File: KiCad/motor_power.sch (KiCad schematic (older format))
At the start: 28 parts

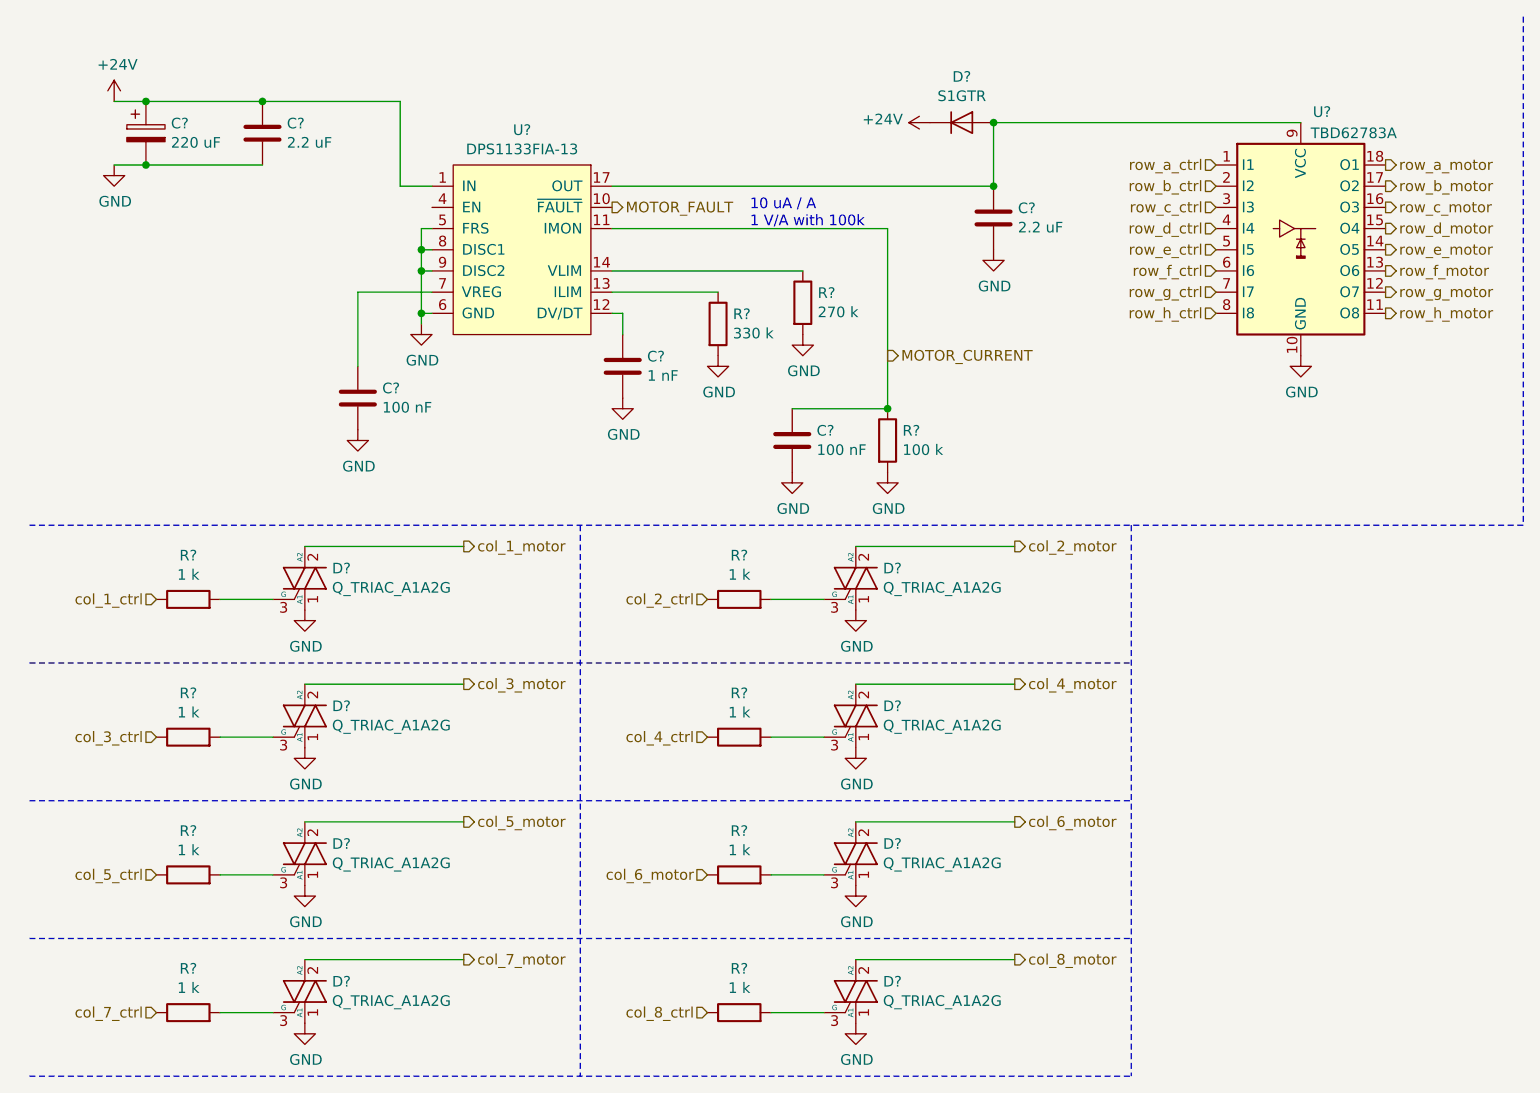
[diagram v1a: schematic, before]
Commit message: Fixing ERC rules
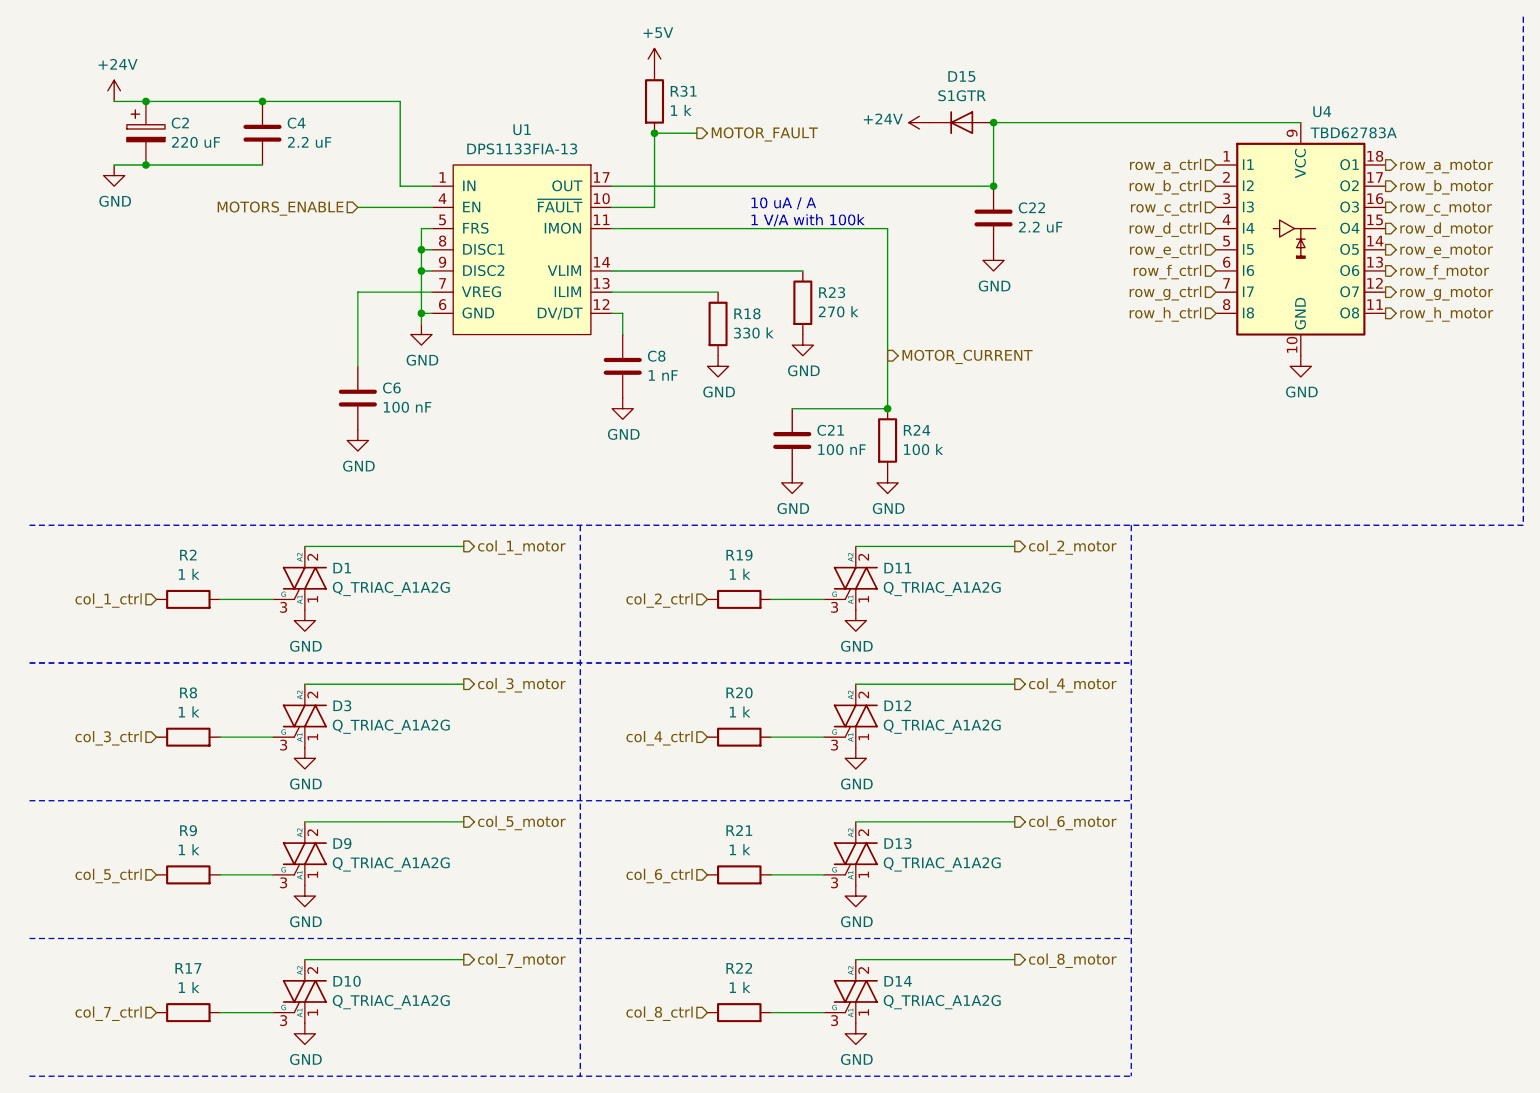
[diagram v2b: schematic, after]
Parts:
- added R31: 1 k, symbol Device:R
- gave numbers to parts that had none: 28
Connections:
- net MOTOR_FAULT: now also R31.2
- net col_6_motor: no longer R21.1
- net MOTORS_ENABLE: now reaches U1.4 (EN)
- new net +5V: R31.1
- new net col_6_ctrl: R21.1

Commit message: Current WIP for board layout
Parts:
- removed C2: 220 uF, symbol Device:CP
- added C2: 22 uF, Capacitor_SMD:C_1210_3225Metric_Pad1.42x2.65mm_HandSolder, symbol Device:C
- C21, C22, C4, C6, C8: footprint (none) -> Capacitor_SMD:C_0603_1608Metric_Pad1.05x0.95mm_HandSolder
- D1, D10, D11, D12, D13, D14, D3, D9: footprint (none) -> Package_TO_SOT_SMD:SOT-223-3_TabPin2
- D15: footprint (none) -> Diode_SMD:D_SMA_Handsoldering
- R17, R18, R19, R2, R20, R21, R22, R23, R24, R31, R8, R9: footprint (none) -> Resistor_SMD:R_0603_1608Metric_Pad1.05x0.95mm_HandSolder
- U1: footprint kicad_pcb:QFN-17-Diodes1 -> Snack Machine:DPS1133FIA-13
- U4: footprint (none) -> Package_SO:SSOP-18_4.4x6.5mm_P0.65mm
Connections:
- net +24V: now also C2.1
- net GND: now also C2.2
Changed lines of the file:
@@
 F 0 "U4" H 6550 2000 50  0000 C CNN
 F 1 "TBD62783A" H 6700 1900 50  0000 C CNN
-F 2 "" H 6450 900 50  0001 C CNN
+F 2 "Package_SO:SSOP-18_4.4x6.5mm_P0.65mm" H 6450 900 50  0001 C CNN
 F 3 "http://toshiba.semicon-storage.com/info/docget.jsp?did=30523&prodName=TBD62783APG" H 6150 1850 50  0001 C CNN
 	1    6450 1450
@@
 F 0 "U1" H 2775 1315 50  0000 C CNN
 F 1 "DPS1133FIA-13" H 2775 1224 50  0000 C CNN
-F 2 "kicad_pcb:QFN-17-Diodes1" H 2450 1200 50  0001 L CNN
+F 2 "Snack Machine:DPS1133FIA-13" H 2450 1200 50  0001 L CNN
 F 3 "" V 2700 1150 50  0001 C CNN
 	1    2450 1150
@@
 F 0 "C4" H 1665 1046 50  0000 L CNN
 F 1 "2.2 uF" H 1665 955 50  0000 L CNN
-F 2 "" H 1588 850 50  0001 C CNN
+F 2 "Capacitor_SMD:C_0603_1608Metric_Pad1.05x0.95mm_HandSolder" H 1588 850 50  0001 C CNN
 F 3 "~" H 1550 1000 50  0001 C CNN
 	1    1550 1000
@@
 $EndComp
 Wire Wire Line
-	850  850  1000 850
-Wire Wire Line
-	850  1150 1000 1150
-$Comp
-L Device:CP C2
-U 1 1 5DBC5CDD
-P 1000 1000
-F 0 "C2" H 1118 1046 50  0000 L CNN
-F 1 "220 uF" H 1118 955 50  0000 L CNN
-F 2 "" H 1038 850 50  0001 C CNN
-F 3 "~" H 1000 1000 50  0001 C CNN
-	1    1000 1000
-	1    0    0    -1
-$EndComp
-Connection ~ 1000 850
-Wire Wire Line
-	1000 850  1550 850
-Connection ~ 1000 1150
-Wire Wire Line
-	1000 1150 1550 1150
-Wire Wire Line
 	1550 850  2200 850
 Wire Wire Line
@@
 F 0 "C6" H 2115 2296 50  0000 L CNN
 F 1 "100 nF" H 2115 2205 50  0000 L CNN
-F 2 "" H 2038 2100 50  0001 C CNN
+F 2 "Capacitor_SMD:C_0603_1608Metric_Pad1.05x0.95mm_HandSolder" H 2038 2100 50  0001 C CNN
 F 3 "~" H 2000 2250 50  0001 C CNN
 	1    2000 2250
@@
 F 0 "C8" H 3365 2146 50  0000 L CNN
 F 1 "1 nF" H 3365 2055 50  0000 L CNN
-F 2 "" H 3288 1950 50  0001 C CNN
+F 2 "Capacitor_SMD:C_0603_1608Metric_Pad1.05x0.95mm_HandSolder" H 3288 1950 50  0001 C CNN
 F 3 "~" H 3250 2100 50  0001 C CNN
 	1    3250 2100
@@
 F 0 "R18" H 3770 1946 50  0000 L CNN
 F 1 "330 k" H 3770 1855 50  0000 L CNN
-F 2 "" V 3630 1900 50  0001 C CNN
+F 2 "Resistor_SMD:R_0603_1608Metric_Pad1.05x0.95mm_HandSolder" V 3630 1900 50  0001 C CNN
 F 3 "~" H 3700 1900 50  0001 C CNN
 	1    3700 1900
@@
 F 0 "R23" H 4170 1846 50  0000 L CNN
 F 1 "270 k" H 4170 1755 50  0000 L CNN
-F 2 "" V 4030 1800 50  0001 C CNN
+F 2 "Resistor_SMD:R_0603_1608Metric_Pad1.05x0.95mm_HandSolder" V 4030 1800 50  0001 C CNN
 F 3 "~" H 4100 1800 50  0001 C CNN
 	1    4100 1800
@@
 F 0 "R24" H 4570 2496 50  0000 L CNN
 F 1 "100 k" H 4570 2405 50  0000 L CNN
-F 2 "" V 4430 2450 50  0001 C CNN
+F 2 "Resistor_SMD:R_0603_1608Metric_Pad1.05x0.95mm_HandSolder" V 4430 2450 50  0001 C CNN
 F 3 "~" H 4500 2450 50  0001 C CNN
 	1    4500 2450
@@
 F 0 "C21" H 4165 2496 50  0000 L CNN
 F 1 "100 nF" H 4165 2405 50  0000 L CNN
-F 2 "" H 4088 2300 50  0001 C CNN
+F 2 "Capacitor_SMD:C_0603_1608Metric_Pad1.05x0.95mm_HandSolder" H 4088 2300 50  0001 C CNN
 F 3 "~" H 4050 2450 50  0001 C CNN
 	1    4050 2450
@@
 F 0 "D15" H 4850 1166 50  0000 C CNN
 F 1 "S1GTR" H 4850 1075 50  0000 C CNN
-F 2 "" H 4850 950 50  0001 C CNN
+F 2 "Diode_SMD:D_SMA_Handsoldering" H 4850 950 50  0001 C CNN
 F 3 "~" H 4850 950 50  0001 C CNN
 	1    4850 950
@@
 F 0 "C22" H 5115 1446 50  0000 L CNN
 F 1 "2.2 uF" H 5115 1355 50  0000 L CNN
-F 2 "" H 5038 1250 50  0001 C CNN
+F 2 "Capacitor_SMD:C_0603_1608Metric_Pad1.05x0.95mm_HandSolder" H 5038 1250 50  0001 C CNN
 F 3 "~" H 5000 1400 50  0001 C CNN
 	1    5000 1400
@@
 F 0 "D1" H 1878 3146 50  0000 L CNN
 F 1 "Q_TRIAC_A1A2G" H 1878 3055 50  0000 L CNN
-F 2 "" V 1825 3125 50  0001 C CNN
+F 2 "Package_TO_SOT_SMD:SOT-223-3_TabPin2" V 1825 3125 50  0001 C CNN
 F 3 "~" V 1750 3100 50  0001 C CNN
 	1    1750 3100
@@
 F 0 "R2" V 1407 3200 50  0000 C CNN
 F 1 "1 k" V 1316 3200 50  0000 C CNN
-F 2 "" V 1130 3200 50  0001 C CNN
+F 2 "Resistor_SMD:R_0603_1608Metric_Pad1.05x0.95mm_HandSolder" V 1130 3200 50  0001 C CNN
 F 3 "~" H 1200 3200 50  0001 C CNN
 	1    1200 3200
@@
 F 0 "D3" H 1878 3796 50  0000 L CNN
 F 1 "Q_TRIAC_A1A2G" H 1878 3705 50  0000 L CNN
-F 2 "" V 1825 3775 50  0001 C CNN
+F 2 "Package_TO_SOT_SMD:SOT-223-3_TabPin2" V 1825 3775 50  0001 C CNN
 F 3 "~" V 1750 3750 50  0001 C CNN
 	1    1750 3750
@@
 F 0 "R8" V 1407 3850 50  0000 C CNN
 F 1 "1 k" V 1316 3850 50  0000 C CNN
-F 2 "" V 1130 3850 50  0001 C CNN
+F 2 "Resistor_SMD:R_0603_1608Metric_Pad1.05x0.95mm_HandSolder" V 1130 3850 50  0001 C CNN
 F 3 "~" H 1200 3850 50  0001 C CNN
 	1    1200 3850
@@
 F 0 "D9" H 1878 4446 50  0000 L CNN
 F 1 "Q_TRIAC_A1A2G" H 1878 4355 50  0000 L CNN
-F 2 "" V 1825 4425 50  0001 C CNN
+F 2 "Package_TO_SOT_SMD:SOT-223-3_TabPin2" V 1825 4425 50  0001 C CNN
 F 3 "~" V 1750 4400 50  0001 C CNN
 	1    1750 4400
@@
 F 0 "R9" V 1407 4500 50  0000 C CNN
 F 1 "1 k" V 1316 4500 50  0000 C CNN
-F 2 "" V 1130 4500 50  0001 C CNN
+F 2 "Resistor_SMD:R_0603_1608Metric_Pad1.05x0.95mm_HandSolder" V 1130 4500 50  0001 C CNN
 F 3 "~" H 1200 4500 50  0001 C CNN
 	1    1200 4500
@@
 F 0 "D10" H 1878 5096 50  0000 L CNN
 F 1 "Q_TRIAC_A1A2G" H 1878 5005 50  0000 L CNN
-F 2 "" V 1825 5075 50  0001 C CNN
+F 2 "Package_TO_SOT_SMD:SOT-223-3_TabPin2" V 1825 5075 50  0001 C CNN
 F 3 "~" V 1750 5050 50  0001 C CNN
 	1    1750 5050
@@
 F 0 "R17" V 1407 5150 50  0000 C CNN
 F 1 "1 k" V 1316 5150 50  0000 C CNN
-F 2 "" V 1130 5150 50  0001 C CNN
+F 2 "Resistor_SMD:R_0603_1608Metric_Pad1.05x0.95mm_HandSolder" V 1130 5150 50  0001 C CNN
 F 3 "~" H 1200 5150 50  0001 C CNN
 	1    1200 5150
@@
 F 0 "D11" H 4478 3146 50  0000 L CNN
 F 1 "Q_TRIAC_A1A2G" H 4478 3055 50  0000 L CNN
-F 2 "" V 4425 3125 50  0001 C CNN
+F 2 "Package_TO_SOT_SMD:SOT-223-3_TabPin2" V 4425 3125 50  0001 C CNN
 F 3 "~" V 4350 3100 50  0001 C CNN
 	1    4350 3100
@@
 F 0 "R19" V 4007 3200 50  0000 C CNN
 F 1 "1 k" V 3916 3200 50  0000 C CNN
-F 2 "" V 3730 3200 50  0001 C CNN
+F 2 "Resistor_SMD:R_0603_1608Metric_Pad1.05x0.95mm_HandSolder" V 3730 3200 50  0001 C CNN
 F 3 "~" H 3800 3200 50  0001 C CNN
 	1    3800 3200
@@
 F 0 "D12" H 4478 3796 50  0000 L CNN
 F 1 "Q_TRIAC_A1A2G" H 4478 3705 50  0000 L CNN
-F 2 "" V 4425 3775 50  0001 C CNN
+F 2 "Package_TO_SOT_SMD:SOT-223-3_TabPin2" V 4425 3775 50  0001 C CNN
 F 3 "~" V 4350 3750 50  0001 C CNN
 	1    4350 3750
@@
 F 0 "R20" V 4007 3850 50  0000 C CNN
 F 1 "1 k" V 3916 3850 50  0000 C CNN
-F 2 "" V 3730 3850 50  0001 C CNN
+F 2 "Resistor_SMD:R_0603_1608Metric_Pad1.05x0.95mm_HandSolder" V 3730 3850 50  0001 C CNN
 F 3 "~" H 3800 3850 50  0001 C CNN
 	1    3800 3850
@@
 F 0 "D13" H 4478 4446 50  0000 L CNN
 F 1 "Q_TRIAC_A1A2G" H 4478 4355 50  0000 L CNN
-F 2 "" V 4425 4425 50  0001 C CNN
+F 2 "Package_TO_SOT_SMD:SOT-223-3_TabPin2" V 4425 4425 50  0001 C CNN
 F 3 "~" V 4350 4400 50  0001 C CNN
 	1    4350 4400
@@
 F 0 "R21" V 4007 4500 50  0000 C CNN
 F 1 "1 k" V 3916 4500 50  0000 C CNN
-F 2 "" V 3730 4500 50  0001 C CNN
+F 2 "Resistor_SMD:R_0603_1608Metric_Pad1.05x0.95mm_HandSolder" V 3730 4500 50  0001 C CNN
 F 3 "~" H 3800 4500 50  0001 C CNN
 	1    3800 4500
@@
 F 0 "D14" H 4478 5096 50  0000 L CNN
 F 1 "Q_TRIAC_A1A2G" H 4478 5005 50  0000 L CNN
-F 2 "" V 4425 5075 50  0001 C CNN
+F 2 "Package_TO_SOT_SMD:SOT-223-3_TabPin2" V 4425 5075 50  0001 C CNN
 F 3 "~" V 4350 5050 50  0001 C CNN
 	1    4350 5050
@@
 F 0 "R22" V 4007 5150 50  0000 C CNN
 F 1 "1 k" V 3916 5150 50  0000 C CNN
-F 2 "" V 3730 5150 50  0001 C CNN
+F 2 "Resistor_SMD:R_0603_1608Metric_Pad1.05x0.95mm_HandSolder" V 3730 5150 50  0001 C CNN
 F 3 "~" H 3800 5150 50  0001 C CNN
 	1    3800 5150
@@
 F 0 "R31" H 3470 896 50  0000 L CNN
 F 1 "1 k" H 3470 805 50  0000 L CNN
-F 2 "" V 3330 850 50  0001 C CNN
+F 2 "Resistor_SMD:R_0603_1608Metric_Pad1.05x0.95mm_HandSolder" V 3330 850 50  0001 C CNN
 F 3 "~" H 3400 850 50  0001 C CNN
 	1    3400 850
@@
 Wire Wire Line
 	2000 1350 2350 1350
+Wire Wire Line
+	1000 1150 1550 1150
+Wire Wire Line
+	850  1150 1000 1150
+Connection ~ 1000 1150
+Wire Wire Line
+	1000 850  1550 850
+Wire Wire Line
+	850  850  1000 850
+Connection ~ 1000 850
+$Comp
+L Device:C C2
+U 1 1 5DCB7FDD
+P 1000 1000
+F 0 "C2" H 1115 1046 50  0000 L CNN
+F 1 "22 uF" H 1115 955 50  0000 L CNN
+F 2 "Capacitor_SMD:C_1210_3225Metric_Pad1.42x2.65mm_HandSolder" H 1038 850 50  0001 C CNN
+F 3 "~" H 1000 1000 50  0001 C CNN
+	1    1000 1000
+	1    0    0    -1
+$EndComp
 $EndSCHEMATC

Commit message: Sourcing parts
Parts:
- C2: value 22 uF -> 22uF; Part Number (none) -> GMK325BJ226MM-P
- C21, C6: value 100 nF -> 100nF
- C22, C4: value 2.2 uF -> 2.2uF; Part Number (none) -> C1608JB1V225K080AC
- C8: value 1 nF -> 1nF; Part Number (none) -> C1608C0G1H102J080AA
- R17, R19, R2, R20, R21, R22, R31, R8, R9: value 1 k -> 1k
- R18: value 330 k -> 330k
- R23: value 270 k -> 270k
- R24: value 100 k -> 100k
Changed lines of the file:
@@
 P 1550 1000
 F 0 "C4" H 1665 1046 50  0000 L CNN
-F 1 "2.2 uF" H 1665 955 50  0000 L CNN
+F 1 "2.2uF" H 1665 955 50  0000 L CNN
 F 2 "Capacitor_SMD:C_0603_1608Metric_Pad1.05x0.95mm_HandSolder" H 1588 850 50  0001 C CNN
 F 3 "~" H 1550 1000 50  0001 C CNN
+F 4 "C1608JB1V225K080AC" H 1550 1000 50  0001 C CNN "Part Number"
 	1    1550 1000
 	1    0    0    -1
@@
 P 2000 2250
 F 0 "C6" H 2115 2296 50  0000 L CNN
-F 1 "100 nF" H 2115 2205 50  0000 L CNN
+F 1 "100nF" H 2115 2205 50  0000 L CNN
 F 2 "Capacitor_SMD:C_0603_1608Metric_Pad1.05x0.95mm_HandSolder" H 2038 2100 50  0001 C CNN
 F 3 "~" H 2000 2250 50  0001 C CNN
@@
 P 3250 2100
 F 0 "C8" H 3365 2146 50  0000 L CNN
-F 1 "1 nF" H 3365 2055 50  0000 L CNN
+F 1 "1nF" H 3365 2055 50  0000 L CNN
 F 2 "Capacitor_SMD:C_0603_1608Metric_Pad1.05x0.95mm_HandSolder" H 3288 1950 50  0001 C CNN
 F 3 "~" H 3250 2100 50  0001 C CNN
+F 4 "C1608C0G1H102J080AA" H 3250 2100 50  0001 C CNN "Part Number"
 	1    3250 2100
 	1    0    0    -1
@@
 P 3700 1900
 F 0 "R18" H 3770 1946 50  0000 L CNN
-F 1 "330 k" H 3770 1855 50  0000 L CNN
+F 1 "330k" H 3770 1855 50  0000 L CNN
 F 2 "Resistor_SMD:R_0603_1608Metric_Pad1.05x0.95mm_HandSolder" V 3630 1900 50  0001 C CNN
 F 3 "~" H 3700 1900 50  0001 C CNN
@@
 P 4100 1800
 F 0 "R23" H 4170 1846 50  0000 L CNN
-F 1 "270 k" H 4170 1755 50  0000 L CNN
+F 1 "270k" H 4170 1755 50  0000 L CNN
 F 2 "Resistor_SMD:R_0603_1608Metric_Pad1.05x0.95mm_HandSolder" V 4030 1800 50  0001 C CNN
 F 3 "~" H 4100 1800 50  0001 C CNN
@@
 P 4500 2450
 F 0 "R24" H 4570 2496 50  0000 L CNN
-F 1 "100 k" H 4570 2405 50  0000 L CNN
+F 1 "100k" H 4570 2405 50  0000 L CNN
 F 2 "Resistor_SMD:R_0603_1608Metric_Pad1.05x0.95mm_HandSolder" V 4430 2450 50  0001 C CNN
 F 3 "~" H 4500 2450 50  0001 C CNN
@@
 P 4050 2450
 F 0 "C21" H 4165 2496 50  0000 L CNN
-F 1 "100 nF" H 4165 2405 50  0000 L CNN
+F 1 "100nF" H 4165 2405 50  0000 L CNN
 F 2 "Capacitor_SMD:C_0603_1608Metric_Pad1.05x0.95mm_HandSolder" H 4088 2300 50  0001 C CNN
 F 3 "~" H 4050 2450 50  0001 C CNN
@@
 P 5000 1400
 F 0 "C22" H 5115 1446 50  0000 L CNN
-F 1 "2.2 uF" H 5115 1355 50  0000 L CNN
+F 1 "2.2uF" H 5115 1355 50  0000 L CNN
 F 2 "Capacitor_SMD:C_0603_1608Metric_Pad1.05x0.95mm_HandSolder" H 5038 1250 50  0001 C CNN
 F 3 "~" H 5000 1400 50  0001 C CNN
+F 4 "C1608JB1V225K080AC" H 5000 1400 50  0001 C CNN "Part Number"
 	1    5000 1400
 	1    0    0    -1
@@
 P 1200 3200
 F 0 "R2" V 1407 3200 50  0000 C CNN
-F 1 "1 k" V 1316 3200 50  0000 C CNN
+F 1 "1k" V 1316 3200 50  0000 C CNN
 F 2 "Resistor_SMD:R_0603_1608Metric_Pad1.05x0.95mm_HandSolder" V 1130 3200 50  0001 C CNN
 F 3 "~" H 1200 3200 50  0001 C CNN
@@
 P 1200 3850
 F 0 "R8" V 1407 3850 50  0000 C CNN
-F 1 "1 k" V 1316 3850 50  0000 C CNN
+F 1 "1k" V 1316 3850 50  0000 C CNN
 F 2 "Resistor_SMD:R_0603_1608Metric_Pad1.05x0.95mm_HandSolder" V 1130 3850 50  0001 C CNN
 F 3 "~" H 1200 3850 50  0001 C CNN
@@
 P 1200 4500
 F 0 "R9" V 1407 4500 50  0000 C CNN
-F 1 "1 k" V 1316 4500 50  0000 C CNN
+F 1 "1k" V 1316 4500 50  0000 C CNN
 F 2 "Resistor_SMD:R_0603_1608Metric_Pad1.05x0.95mm_HandSolder" V 1130 4500 50  0001 C CNN
 F 3 "~" H 1200 4500 50  0001 C CNN
@@
 P 1200 5150
 F 0 "R17" V 1407 5150 50  0000 C CNN
-F 1 "1 k" V 1316 5150 50  0000 C CNN
+F 1 "1k" V 1316 5150 50  0000 C CNN
 F 2 "Resistor_SMD:R_0603_1608Metric_Pad1.05x0.95mm_HandSolder" V 1130 5150 50  0001 C CNN
 F 3 "~" H 1200 5150 50  0001 C CNN
@@
 P 3800 3200
 F 0 "R19" V 4007 3200 50  0000 C CNN
-F 1 "1 k" V 3916 3200 50  0000 C CNN
+F 1 "1k" V 3916 3200 50  0000 C CNN
 F 2 "Resistor_SMD:R_0603_1608Metric_Pad1.05x0.95mm_HandSolder" V 3730 3200 50  0001 C CNN
 F 3 "~" H 3800 3200 50  0001 C CNN
@@
 P 3800 3850
 F 0 "R20" V 4007 3850 50  0000 C CNN
-F 1 "1 k" V 3916 3850 50  0000 C CNN
+F 1 "1k" V 3916 3850 50  0000 C CNN
 F 2 "Resistor_SMD:R_0603_1608Metric_Pad1.05x0.95mm_HandSolder" V 3730 3850 50  0001 C CNN
 F 3 "~" H 3800 3850 50  0001 C CNN
@@
 P 3800 4500
 F 0 "R21" V 4007 4500 50  0000 C CNN
-F 1 "1 k" V 3916 4500 50  0000 C CNN
+F 1 "1k" V 3916 4500 50  0000 C CNN
 F 2 "Resistor_SMD:R_0603_1608Metric_Pad1.05x0.95mm_HandSolder" V 3730 4500 50  0001 C CNN
 F 3 "~" H 3800 4500 50  0001 C CNN
@@
 P 3800 5150
 F 0 "R22" V 4007 5150 50  0000 C CNN
-F 1 "1 k" V 3916 5150 50  0000 C CNN
+F 1 "1k" V 3916 5150 50  0000 C CNN
 F 2 "Resistor_SMD:R_0603_1608Metric_Pad1.05x0.95mm_HandSolder" V 3730 5150 50  0001 C CNN
 F 3 "~" H 3800 5150 50  0001 C CNN
@@
 P 3400 850
 F 0 "R31" H 3470 896 50  0000 L CNN
-F 1 "1 k" H 3470 805 50  0000 L CNN
+F 1 "1k" H 3470 805 50  0000 L CNN
 F 2 "Resistor_SMD:R_0603_1608Metric_Pad1.05x0.95mm_HandSolder" V 3330 850 50  0001 C CNN
 F 3 "~" H 3400 850 50  0001 C CNN
@@
 P 1000 1000
 F 0 "C2" H 1115 1046 50  0000 L CNN
-F 1 "22 uF" H 1115 955 50  0000 L CNN
+F 1 "22uF" H 1115 955 50  0000 L CNN
 F 2 "Capacitor_SMD:C_1210_3225Metric_Pad1.42x2.65mm_HandSolder" H 1038 850 50  0001 C CNN
 F 3 "~" H 1000 1000 50  0001 C CNN
+F 4 "GMK325BJ226MM-P" H 1000 1000 50  0001 C CNN "Part Number"
 	1    1000 1000
 	1    0    0    -1
